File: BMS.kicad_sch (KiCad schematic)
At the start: 115 parts, among them J1 Conn_01x06_Pin, J2 Conn_01x02_Pin, J5 Conn_01x02_Pin, J6 Conn_01x04_Pin, J7 USB_C_Receptacle_USB2.0_16P, Q1 MMFTP3401-AQ, Q3 SS8050, Q4 IRLZ44N, Q5 IRLZ44N, Q6 IRLZ44N, Q7 IRF4905, Q8 IRF4905, Q9 SS8050, SW3 SW_Push, SW4 SW_Push, U1 USBLC6-2SC6, U11 INA213AIDCKT, U12 SFH617A-3X007T, U13 SFH617A-3X007T, U2 LM2596T-5, U3 ESP32-WROOM-32E, U4 LD1086DT33TR, U5 CH340C, U6 SFH617A-3X007T, U7 SFH617A-3X007T, U8 SFH617A-3X007T, U9 LM324

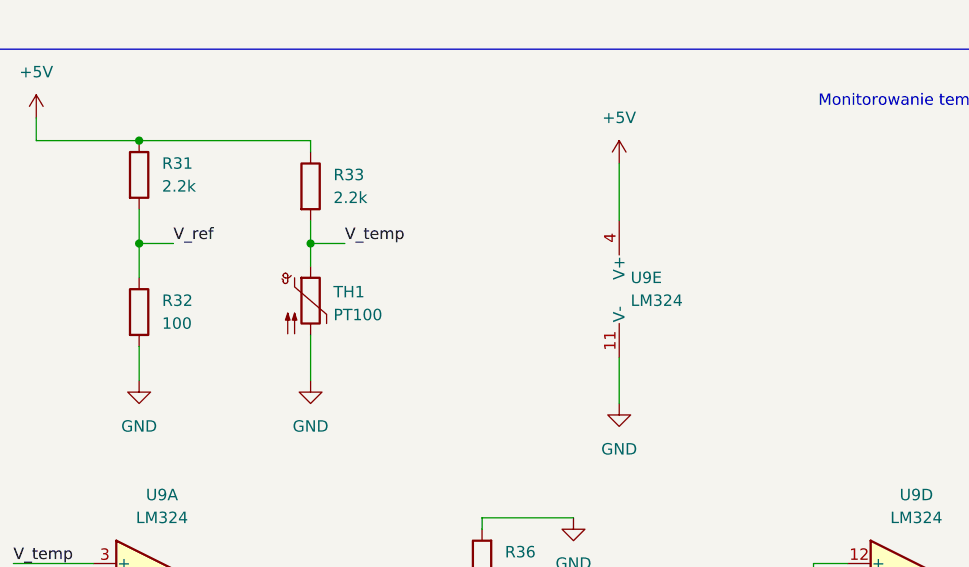
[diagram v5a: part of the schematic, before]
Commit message: rezystory po 100 ohm do pt100
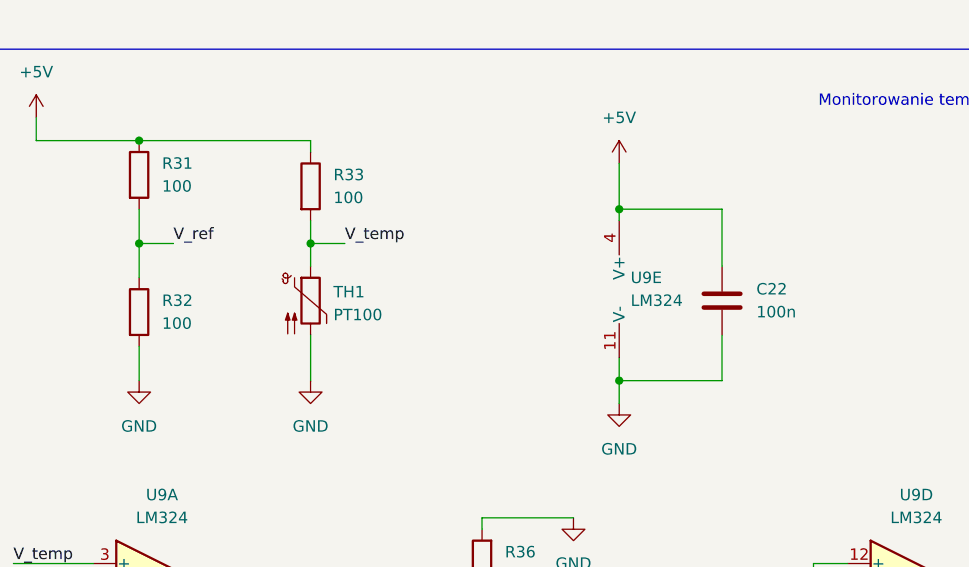
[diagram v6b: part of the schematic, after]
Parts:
- added C22: 100n, Capacitor_SMD:C_0805_2012Metric_Pad1.18x1.45mm_HandSolder, symbol Device:C
- R31, R33: value 2.2k -> 100
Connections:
- net +5V: now also C22.1
- net GND: now also C22.2
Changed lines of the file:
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@@
 	)
 	(junction
+		(at 303.53 171.45)
+		(diameter 0)
+		(color 0 0 0 0)
+	)
+	(junction
 		(at 397.51 201.93)
 		(diameter 0)
@@
 	)
 	(junction
+		(at 303.53 190.5)
+		(diameter 0)
+		(color 0 0 0 0)
+	)
+	(junction
 		(at 64.77 81.28)
 		(diameter 0)
@@
 	(wire
 		(pts
+			(xy 314.96 185.42) (xy 314.96 190.5)
+		)
+		(stroke
+			(width 0)
+			(type default)
+		)
+	)
+	(wire
+		(pts
 			(xy 49.53 63.5) (xy 53.34 63.5)
 		)
@@
 	(wire
 		(pts
-			(xy 303.53 187.96) (xy 303.53 193.04)
+			(xy 303.53 187.96) (xy 303.53 190.5)
 		)
 		(stroke
@@
 	(wire
 		(pts
+			(xy 314.96 177.8) (xy 314.96 171.45)
+		)
+		(stroke
+			(width 0)
+			(type default)
+		)
+	)
+	(wire
+		(pts
 			(xy 88.9 78.74) (xy 88.9 81.28)
 		)
@@
 	(wire
 		(pts
+			(xy 303.53 171.45) (xy 303.53 172.72)
+		)
+		(stroke
+			(width 0)
+			(type default)
+		)
+	)
+	(wire
+		(pts
 			(xy 185.42 220.98) (xy 185.42 223.52)
 		)
@@
 	(wire
 		(pts
+			(xy 314.96 190.5) (xy 303.53 190.5)
+		)
+		(stroke
+			(width 0)
+			(type default)
+		)
+	)
+	(wire
+		(pts
 			(xy 209.55 234.95) (xy 219.71 234.95)
 		)
@@
 	(wire
 		(pts
-			(xy 303.53 166.37) (xy 303.53 172.72)
+			(xy 303.53 166.37) (xy 303.53 171.45)
 		)
 		(stroke
@@
 	(wire
 		(pts
+			(xy 314.96 171.45) (xy 303.53 171.45)
+		)
+		(stroke
+			(width 0)
+			(type default)
+		)
+	)
+	(wire
+		(pts
 			(xy 74.93 104.14) (xy 86.36 104.14)
 		)
@@
 	(wire
 		(pts
+			(xy 303.53 190.5) (xy 303.53 193.04)
+		)
+		(stroke
+			(width 0)
+			(type default)
+		)
+	)
+	(wire
+		(pts
 			(xy 209.55 247.65) (xy 209.55 250.19)
 		)
@@
 	)
 	(symbol
+		(lib_id "Device:C")
+		(at 314.96 181.61 0)
+		(unit 1)
+		(body_style 1)
+		(exclude_from_sim no)
+		(in_bom yes)
+		(on_board yes)
+		(in_pos_files yes)
+		(dnp no)
+		(fields_autoplaced yes)
+		(property "Reference" "C22"
+			(at 318.77 180.3399 0)
+			(show_name no)
+			(do_not_autoplace no)
+			(effects
+				(font
+					(size 1.27 1.27)
+				)
+				(justify left)
+			)
+		)
+		(property "Value" "100n"
+			(at 318.77 182.8799 0)
+			(show_name no)
+			(do_not_autoplace no)
+			(effects
+				(font
+					(size 1.27 1.27)
+				)
+				(justify left)
+			)
+		)
+		(property "Footprint" "Capacitor_SMD:C_0805_2012Metric_Pad1.18x1.45mm_HandSolder"
+			(at 315.9252 185.42 0)
+			(hide yes)
+			(show_name no)
+			(do_not_autoplace no)
+			(effects
+				(font
+					(size 1.27 1.27)
+				)
+			)
+		)
+		(property "Datasheet" ""
+			(at 314.96 181.61 0)
+			(hide yes)
+			(show_name no)
+			(do_not_autoplace no)
+			(effects
+				(font
+					(size 1.27 1.27)
+				)
+			)
+		)
+		(property "Description" "Unpolarized capacitor"
+			(at 314.96 181.61 0)
+			(hide yes)
+			(show_name no)
+			(do_not_autoplace no)
+			(effects
+				(font
+					(size 1.27 1.27)
+				)
+			)
+		)
+		(pin "1"
+		)
+		(pin "2"
+		)
+		(instances
+			(project "BMS"
+				(path "/416cad80-5d16-4386-bcbd-118262b7dc4e"
+					(reference "C22")
+					(unit 1)
+				)
+			)
+		)
+	)
+	(symbol
 		(lib_id "power:PWR_FLAG")
 		(at 64.77 81.28 0)
@@
 			)
 		)
-		(property "Value" "2.2k"
+		(property "Value" "100"
 			(at 252.73 168.9099 0)
 			(show_name no)
@@
 			)
 		)
-		(property "Value" "2.2k"
+		(property "Value" "100"
 			(at 271.78 170.1799 0)
 			(show_name no)

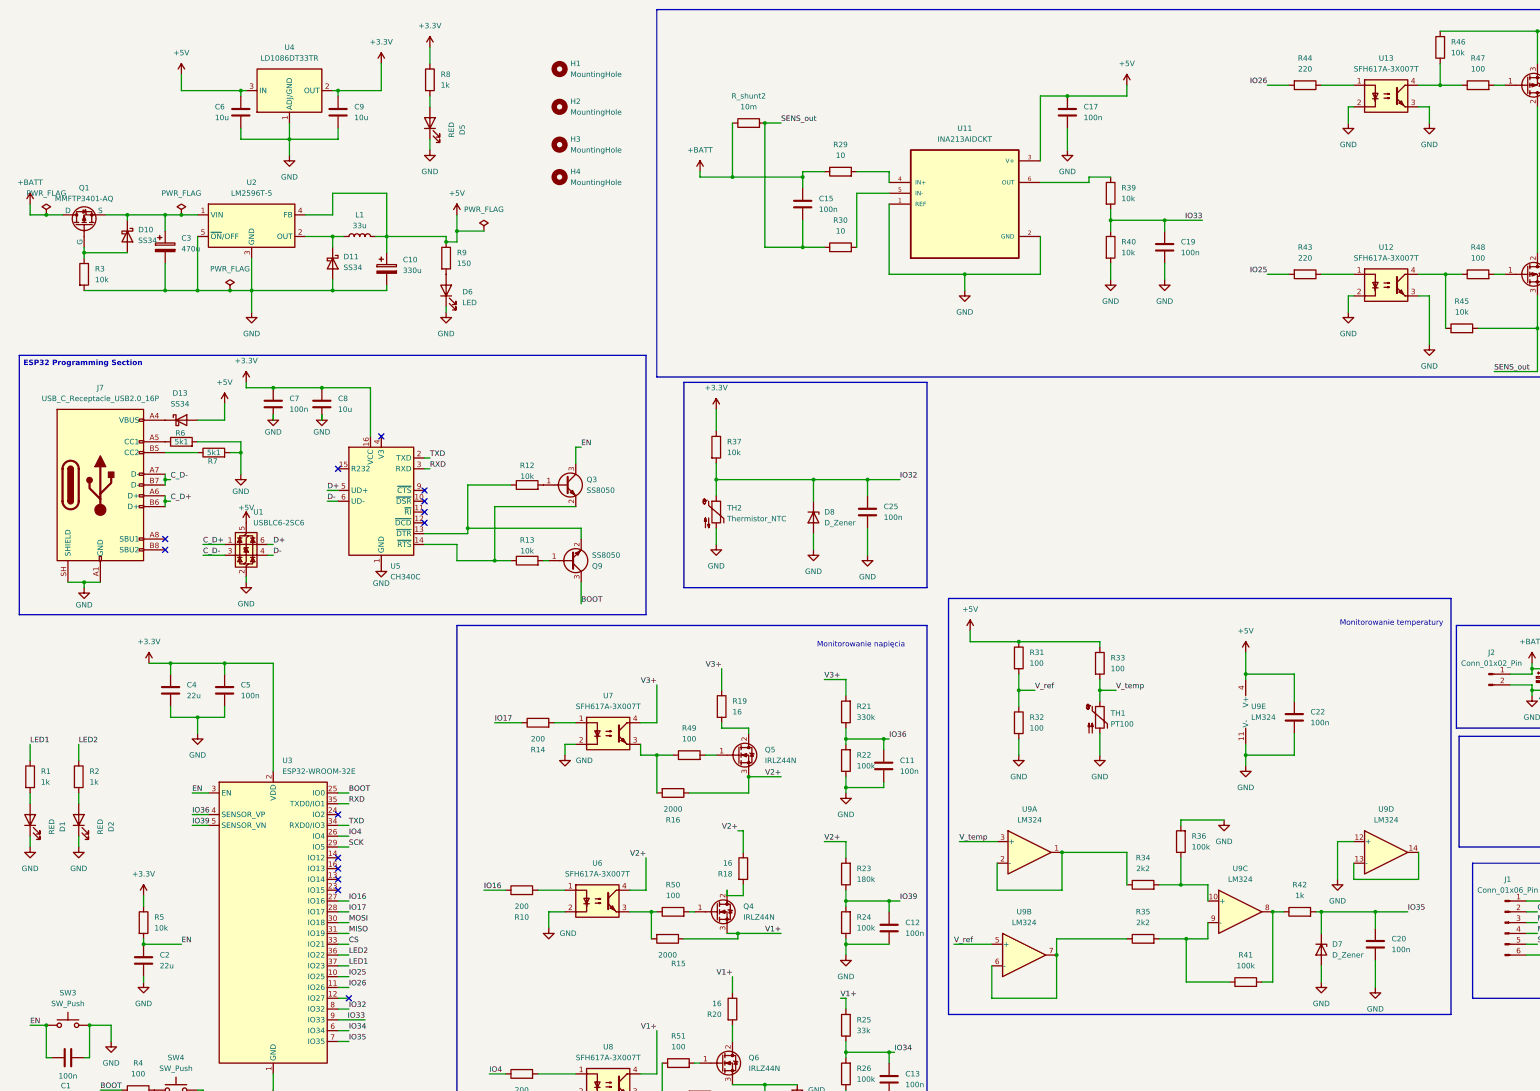
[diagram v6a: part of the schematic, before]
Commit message: Dodanie resystora do PT100
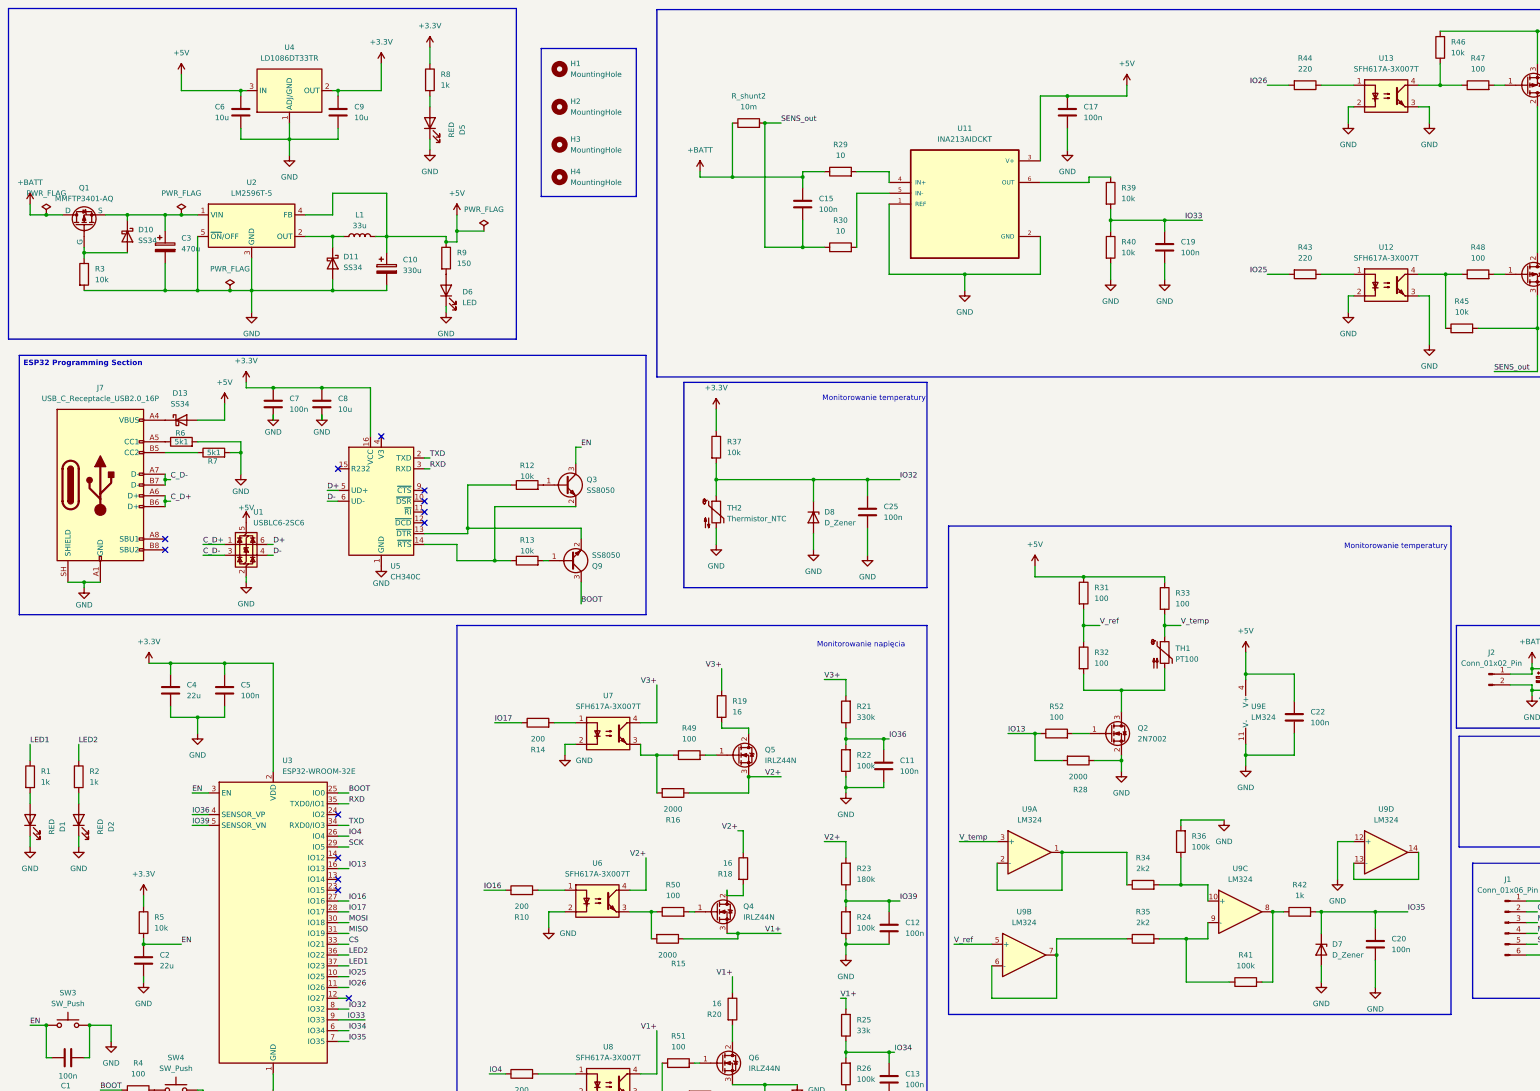
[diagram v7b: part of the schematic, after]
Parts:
- added Q2: 2N7002, Package_TO_SOT_SMD:SOT-23_Handsoldering, symbol Transistor_FET:2N7002
- added R28: 2000, Resistor_SMD:R_0805_2012Metric_Pad1.20x1.40mm_HandSolder, symbol Device:R
- added R52: 100, Resistor_SMD:R_0805_2012Metric_Pad1.20x1.40mm_HandSolder, symbol Device:R
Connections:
- net GND: now also Q2.2 (S), R28.1; no longer R32.2, TH1.2
- net IO13: now reaches U3.16 (IO13)
- net IO13: now also R28.2, R52.1
- new net: Q2.3 (D), R32.2, TH1.2
- new net: Q2.1 (G), R52.2
- no-connect marks 14 -> 13
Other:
- moved on the sheet: R31, R32, R33, TH1

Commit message: L1_47u
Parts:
- L1: value 33u -> 47u
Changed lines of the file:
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@@
 			)
 		)
-		(property "Value" "33u"
+		(property "Value" "47u"
 			(at 95.25 66.04 90)
 			(show_name no)
